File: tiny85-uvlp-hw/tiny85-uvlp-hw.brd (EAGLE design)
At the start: 36.5 x 21.6 mm, 10 parts, among them J1 AVR_SPI, Q1 NFET, U1 TINY85-20-DIP

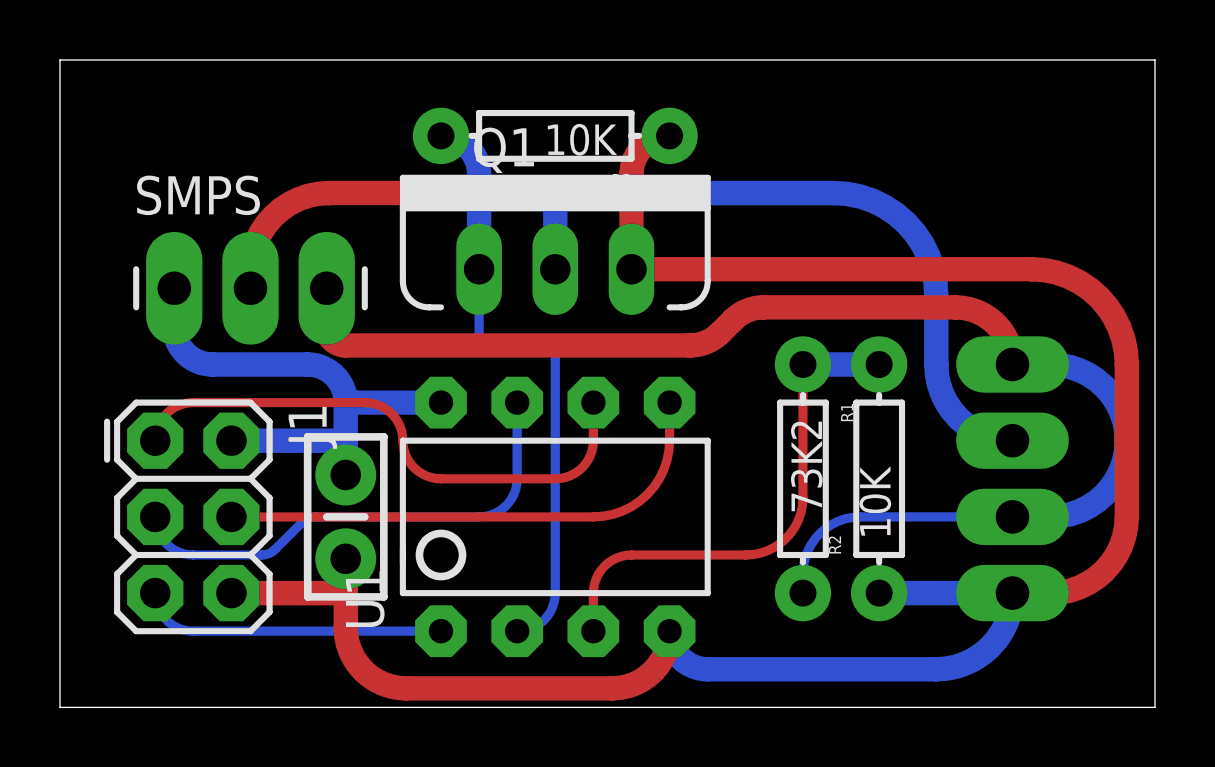
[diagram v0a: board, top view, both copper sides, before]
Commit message: fine tune schematic and routing
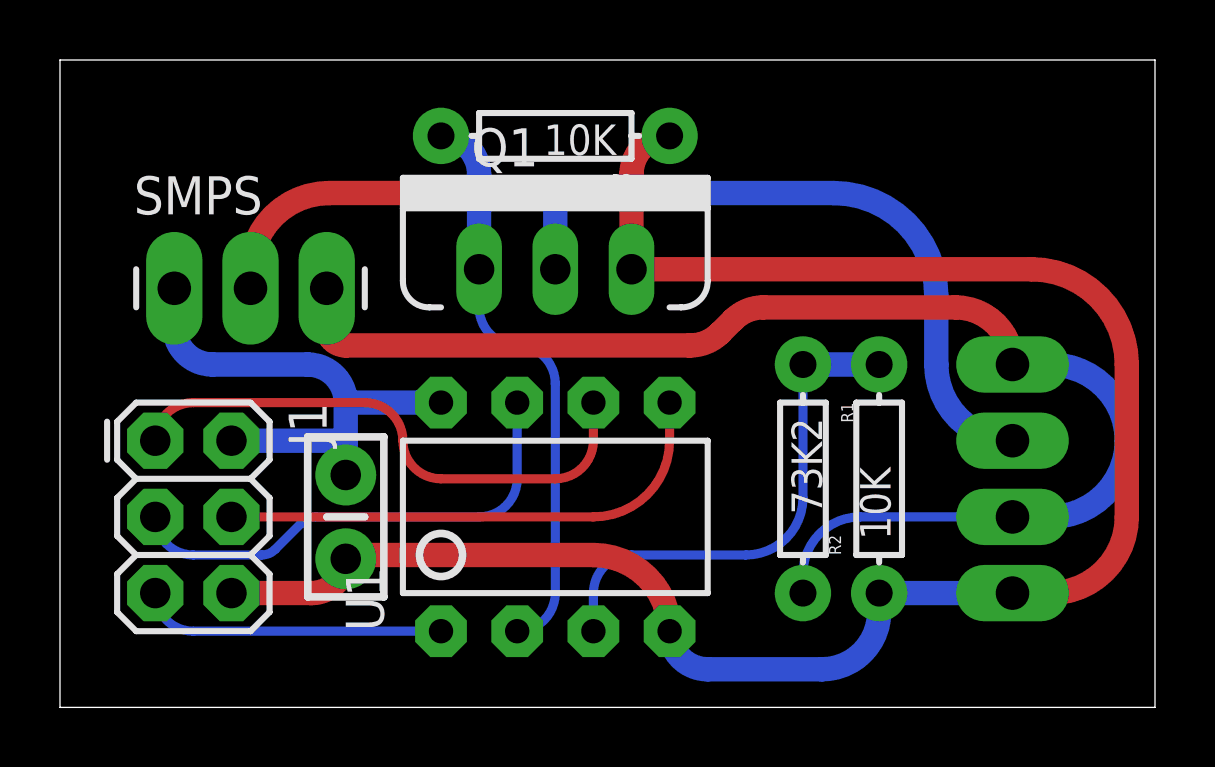
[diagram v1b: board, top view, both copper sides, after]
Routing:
- net GND: track 83.1 -> 76.7 mm
- net GATE: track 20.1 -> 18.6 mm
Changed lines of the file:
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@@
 <wire x1="27.305" y1="3.81" x2="31.75" y2="3.81" width="0.8128" layer="16"/>
 <wire x1="20.32" y1="2.54" x2="21.59" y2="1.27" width="0.8128" layer="16" curve="90"/>
-<wire x1="21.59" y1="1.27" x2="29.21" y2="1.27" width="0.8128" layer="16"/>
-<wire x1="29.21" y1="1.27" x2="31.75" y2="3.81" width="0.8128" layer="16" curve="90"/>
 <wire x1="19.05" y1="14.605" x2="32.385" y2="14.605" width="0.8128" layer="1"/>
 <wire x1="32.385" y1="14.605" x2="35.56" y2="11.43" width="0.8128" layer="1" curve="-90"/>
@@
 <wire x1="19.05" y1="17.78" x2="19.05" y2="17.145" width="0.8128" layer="1"/>
 <wire x1="19.05" y1="17.145" x2="19.05" y2="14.605" width="0.8128" layer="1"/>
-<wire x1="9.525" y1="4.953" x2="9.525" y2="3.81" width="0.8128" layer="1"/>
-<wire x1="9.525" y1="3.81" x2="9.525" y2="2.64304375" width="0.8128" layer="1"/>
-<wire x1="9.525" y1="2.64304375" x2="11.53304375" y2="0.635" width="0.8128" layer="1" curve="90"/>
-<wire x1="11.53304375" y1="0.635" x2="18.415" y2="0.635" width="0.8128" layer="1"/>
-<wire x1="18.415" y1="0.635" x2="20.32" y2="2.54" width="0.8128" layer="1" curve="90"/>
-<wire x1="5.715" y1="3.81" x2="9.525" y2="3.81" width="0.8128" layer="1"/>
+<wire x1="5.715" y1="3.81" x2="8.382" y2="3.81" width="0.8128" layer="1"/>
+<wire x1="8.382" y1="3.81" x2="9.525" y2="4.953" width="0.8128" layer="1" curve="90"/>
 <wire x1="6.35" y1="13.97" x2="6.35" y2="14.526828125" width="0.8128" layer="1"/>
 <wire x1="6.35" y1="14.526828125" x2="8.968171875" y2="17.145" width="0.8128" layer="1" curve="-90"/>
 <wire x1="8.968171875" y1="17.145" x2="19.05" y2="17.145" width="0.8128" layer="1"/>
+<wire x1="20.32" y1="2.54" x2="17.78" y2="5.08" width="0.8128" layer="1" curve="90"/>
+<wire x1="17.78" y1="5.08" x2="9.525" y2="5.08" width="0.8128" layer="1"/>
+<wire x1="9.525" y1="5.08" x2="9.525" y2="4.953" width="0.8128" layer="1"/>
+<wire x1="21.59" y1="1.27" x2="25.4" y2="1.27" width="0.8128" layer="16"/>
+<wire x1="25.4" y1="1.27" x2="27.305" y2="3.175" width="0.8128" layer="16" curve="90"/>
+<wire x1="27.305" y1="3.175" x2="27.305" y2="3.81" width="0.8128" layer="16"/>
 </signal>
 <signal name="+5V">
@@
 <contactref element="U1" pad="3"/>
 <wire x1="27.305" y1="11.43" x2="24.765" y2="11.43" width="0.8128" layer="16"/>
-<wire x1="17.78" y1="2.54" x2="17.78" y2="3.81" width="0.3048" layer="1"/>
-<wire x1="17.78" y1="3.81" x2="19.05" y2="5.08" width="0.3048" layer="1" curve="-90"/>
-<wire x1="19.05" y1="5.08" x2="22.86" y2="5.08" width="0.3048" layer="1"/>
-<wire x1="22.86" y1="5.08" x2="24.765" y2="6.985" width="0.3048" layer="1" curve="90"/>
-<wire x1="24.765" y1="6.985" x2="24.765" y2="11.43" width="0.3048" layer="1"/>
+<wire x1="17.78" y1="2.54" x2="17.78" y2="3.81" width="0.3048" layer="16"/>
+<wire x1="17.78" y1="3.81" x2="19.05" y2="5.08" width="0.3048" layer="16" curve="-90"/>
+<wire x1="19.05" y1="5.08" x2="22.86" y2="5.08" width="0.3048" layer="16"/>
+<wire x1="22.86" y1="5.08" x2="24.765" y2="6.985" width="0.3048" layer="16" curve="90"/>
+<wire x1="24.765" y1="6.985" x2="24.765" y2="11.43" width="0.3048" layer="16"/>
 </signal>
 <signal name="GNDOUT">
@@
 <wire x1="13.97" y1="17.78" x2="13.97" y2="14.605" width="0.8128" layer="16"/>
 <wire x1="15.24" y1="2.54" x2="16.51" y2="3.81" width="0.3048" layer="16" curve="90"/>
-<wire x1="16.51" y1="3.81" x2="16.51" y2="12.065" width="0.3048" layer="16"/>
-<wire x1="16.51" y1="12.065" x2="13.97" y2="12.065" width="0.3048" layer="16"/>
-<wire x1="13.97" y1="12.065" x2="13.97" y2="14.605" width="0.3048" layer="16"/>
+<wire x1="16.51" y1="3.81" x2="16.51" y2="10.795" width="0.3048" layer="16"/>
+<wire x1="16.51" y1="10.795" x2="15.24" y2="12.065" width="0.3048" layer="16" curve="90"/>
+<wire x1="15.24" y1="12.065" x2="13.97" y2="13.335" width="0.3048" layer="16" curve="-90"/>
+<wire x1="13.97" y1="13.335" x2="13.97" y2="14.605" width="0.3048" layer="16"/>
 </signal>
 </signals>
